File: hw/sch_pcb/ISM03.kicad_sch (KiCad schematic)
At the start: 75 parts, among them J1 JUMP_3X2, J13 HEADER_2x01_PARALLEL, J14 HEADER_2x01_PARALLEL, J15 HEADER_2x01_PARALLEL, J16 HEADER_2x01_PARALLEL, J17 HEADER_2x01_PARALLEL, J19 HEADER_2x01_PARALLEL, J2 MCX, J20 HEADER_2x01_PARALLEL, J21 HEADER_2x01_PARALLEL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

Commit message: Routing WiP.
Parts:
- removed J24, J25: HEADER_1x02, Mlab_Pin_Headers:Straight_1x02, symbol MLAB_HEADER:HEADER_1x02
- removed J26: HEADER_2x01_PARALLEL, Mlab_Pin_Headers:Straight_2x01, symbol MLAB_HEADER:HEADER_2x01_PARALLEL
- removed U1: LM1117-3V3, Mlab_IO:SOT-223, symbol MLAB_U:LM1117
- added J6, J7: HEADER_2x01_PARALLEL, Mlab_Pin_Headers:Straight_2x01, symbol MLAB_HEADER:HEADER_2x01_PARALLEL
- added U1: LM1117MP-3.3, Package_TO_SOT_SMD:SOT-223-3_TabPin2, symbol Regulator_Linear:LM1117MP-3.3
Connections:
- net +3.3V: now also U1.2 (VO)
- net GND: now also U1.1 (GND)
- net VCC: now also U1.3 (VI)
- net at R3.1: now also J7.1, J7.2
- net at R2.1: now also J6.1, J6.2
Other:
- note added: "to GPIO2"
- note added: "to GPIO3"
- moved on the sheet: D2, D3, Q1, Q2, R2, R22, R23, R3

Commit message: Roughtly routet PCB.
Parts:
- removed C10: 8,2pF, Capacitor_SMD:C_0805_2012Metric, symbol Device:C_Small
- removed C8: 15pF, Capacitor_SMD:C_0805_2012Metric, symbol Device:C_Small
- removed L2: 0R, Resistor_SMD:R_0805_2012Metric, symbol Device:L_Small
- removed L4, L6: 18nH, Inductor_SMD:L_0805_2012Metric, symbol Device:L_Small
- C11: value 8,2pF -> 9.1pF
- C12: value 2.7pF -> 2.2pF
- C13: value 5.1pF -> 4.7pF
- C4: value 6.8pf -> 10pF
- C6: value 6.8pf -> 100pF
- C7: value 15pF -> 12pF
- C9: value 8,2pF -> 15pF
- L1: value 0R -> 22nH
- L10: value 56nH -> 62nH
- L3: value 18nH -> 36nH
- L5: value 18nH -> 30nH
- L7: value 39nH -> 33nH; UST_ID 5c70984412875079b91f8809 -> (none)
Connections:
- net GND: no longer C6.2
- net at J3.1: now also C6.2
- net at C6.1: now also C12.2, L9.1
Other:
- note added: "Class-E Match Component Values according to AN648 Split TX/RX Board, 434 MHz."
- note added: "Component values according to AN643 Split TX/RX Board"
- note removed: "Component values are optimised for 433MHz"
- moved on the sheet: C6, J17, R13

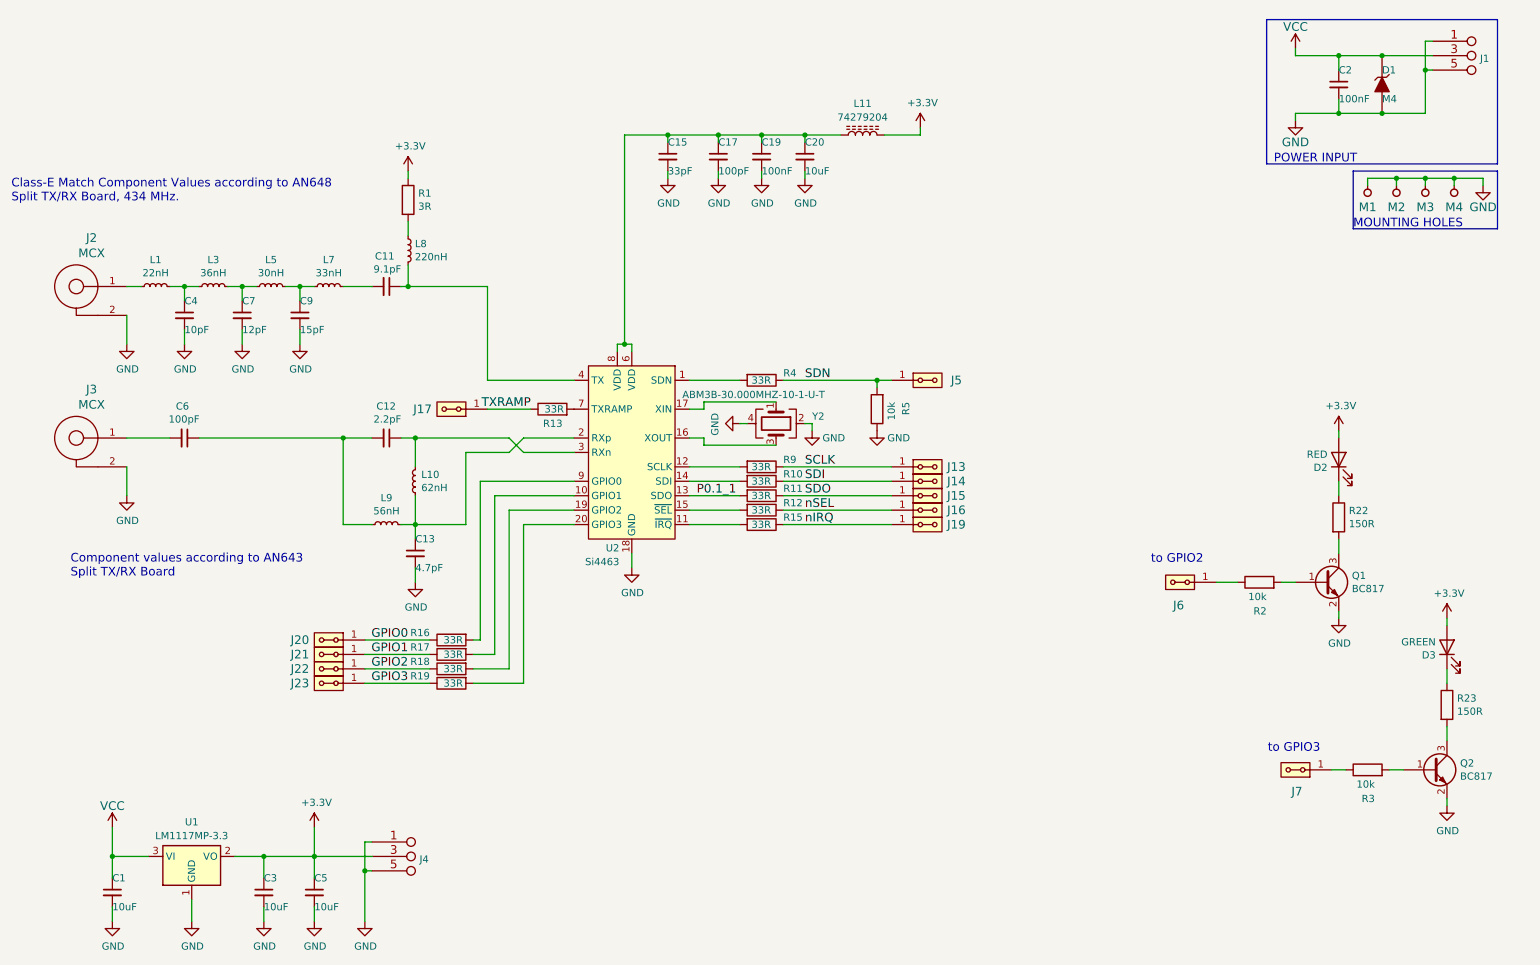
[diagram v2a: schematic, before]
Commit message: Improve Layout, silkscreen Update footprint from libraries.
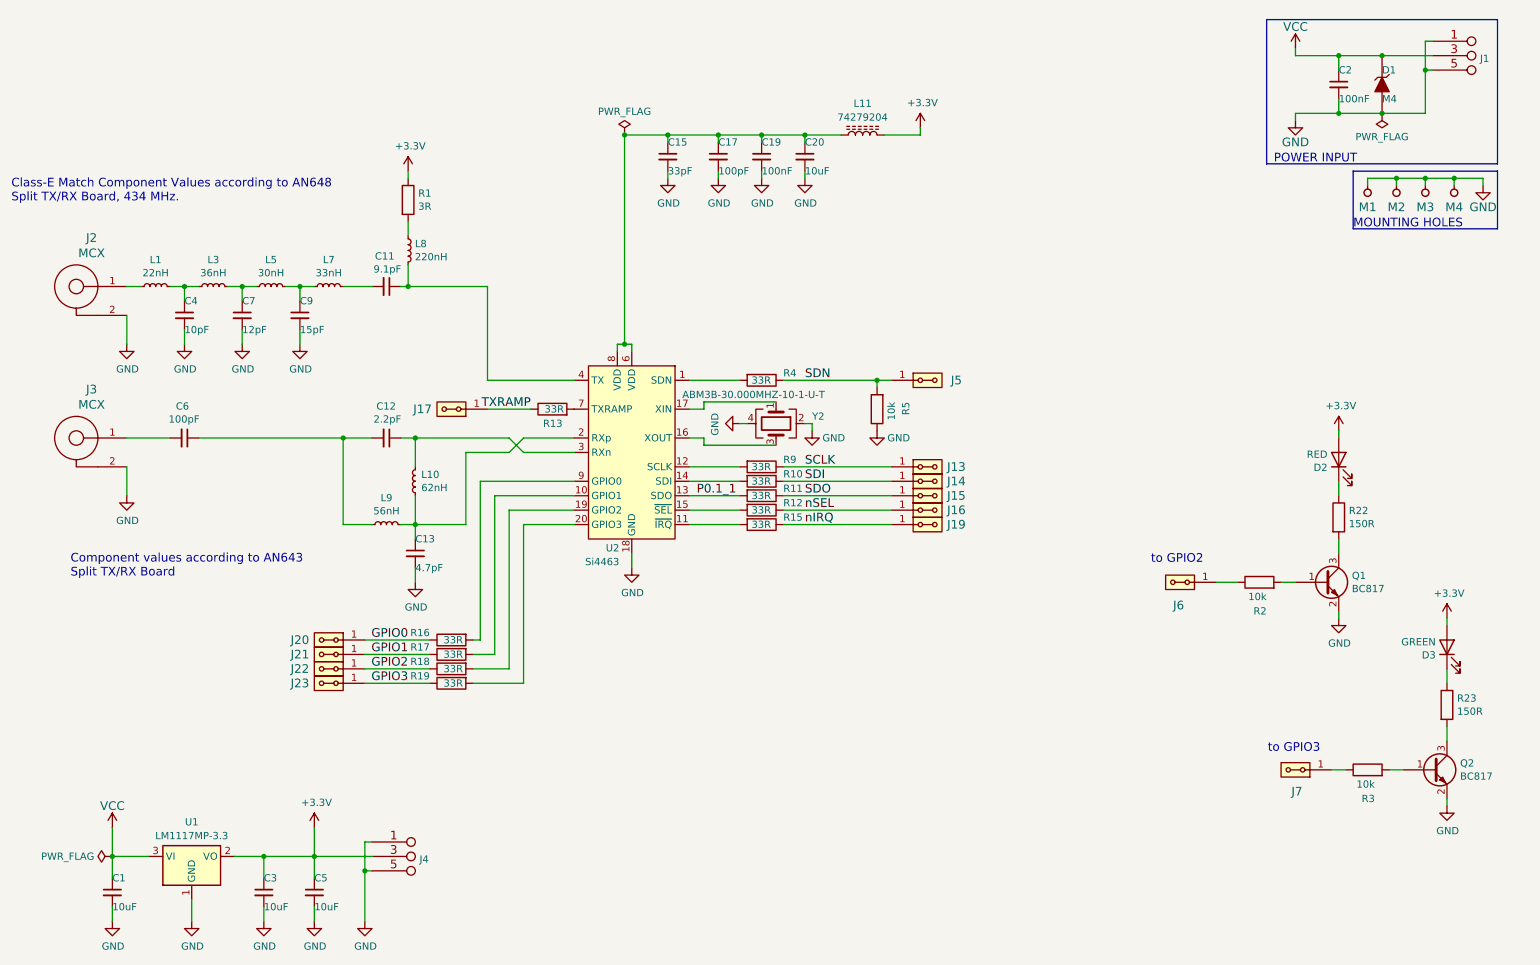
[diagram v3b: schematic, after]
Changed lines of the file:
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@@
 		(rev "ISM01A")
 		(company "Mlab www.mlab.cz")
-		(comment 1 "Sub-GHz ISM radio transceiver")
+		(comment 1 "Sub-GHz ISM radio transceiver\\nwith SPI interface")
 	)
 	(junction
@@
 	)
 	(junction
+		(at 124.46 38.1)
+		(diameter 0)
+		(color 0 0 0 0)
+	)
+	(junction
 		(at 46.99 64.77)
 		(diameter 0)
@@
 	)
 	(symbol
+		(lib_id "power:PWR_FLAG")
+		(at 34.29 165.1 90)
+		(unit 1)
+		(exclude_from_sim no)
+		(in_bom yes)
+		(on_board yes)
+		(dnp no)
+		(fields_autoplaced yes)
+		(property "Reference" "#FLG03"
+			(at 32.385 165.1 0)
+			(effects
+				(font
+					(size 1.27 1.27)
+				)
+				(hide yes)
+			)
+		)
+		(property "Value" "PWR_FLAG"
+			(at 31.1151 165.1 90)
+			(effects
+				(font
+					(size 1.27 1.27)
+				)
+				(justify left)
+			)
+		)
+		(property "Footprint" ""
+			(at 34.29 165.1 0)
+			(effects
+				(font
+					(size 1.27 1.27)
+				)
+				(hide yes)
+			)
+		)
+		(property "Datasheet" "~"
+			(at 34.29 165.1 0)
+			(effects
+				(font
+					(size 1.27 1.27)
+				)
+				(hide yes)
+			)
+		)
+		(property "Description" "Special symbol for telling ERC where power comes from"
+			(at 34.29 165.1 0)
+			(effects
+				(font
+					(size 1.27 1.27)
+				)
+				(hide yes)
+			)
+		)
+		(pin "1"
+		)
+		(instances
+			(project "ISM03"
+				(path "/42713045-fffd-4b2d-ae1e-7232d705fb12"
+					(reference "#FLG03")
+					(unit 1)
+				)
+			)
+		)
+	)
+	(symbol
 		(lib_id "MLAB_HEADER:HEADER_2x01_PARALLEL")
 		(at 222.25 116.84 180)
@@
 	)
 	(symbol
+		(lib_id "power:PWR_FLAG")
+		(at 257.81 34.29 180)
+		(unit 1)
+		(exclude_from_sim no)
+		(in_bom yes)
+		(on_board yes)
+		(dnp no)
+		(fields_autoplaced yes)
+		(property "Reference" "#FLG02"
+			(at 257.81 36.195 0)
+			(effects
+				(font
+					(size 1.27 1.27)
+				)
+				(hide yes)
+			)
+		)
+		(property "Value" "PWR_FLAG"
+			(at 257.81 38.4231 0)
+			(effects
+				(font
+					(size 1.27 1.27)
+				)
+			)
+		)
+		(property "Footprint" ""
+			(at 257.81 34.29 0)
+			(effects
+				(font
+					(size 1.27 1.27)
+				)
+				(hide yes)
+			)
+		)
+		(property "Datasheet" "~"
+			(at 257.81 34.29 0)
+			(effects
+				(font
+					(size 1.27 1.27)
+				)
+				(hide yes)
+			)
+		)
+		(property "Description" "Special symbol for telling ERC where power comes from"
+			(at 257.81 34.29 0)
+			(effects
+				(font
+					(size 1.27 1.27)
+				)
+				(hide yes)
+			)
+		)
+		(pin "1"
+		)
+		(instances
+			(project ""
+				(path "/42713045-fffd-4b2d-ae1e-7232d705fb12"
+					(reference "#FLG02")
+					(unit 1)
+				)
+			)
+		)
+	)
+	(symbol
 		(lib_id "MLAB_HEADER:HEADER_2x01_PARALLEL")
 		(at 177.8 81.28 0)
@@
 					(unit 1)
 				)
+			)
+		)
+	)
+	(symbol
+		(lib_id "power:PWR_FLAG")
+		(at 124.46 38.1 0)
+		(unit 1)
+		(exclude_from_sim no)
+		(in_bom yes)
+		(on_board yes)
+		(dnp no)
+		(fields_autoplaced yes)
+		(property "Reference" "#FLG01"
+			(at 124.46 36.195 0)
+			(effects
+				(font
+					(size 1.27 1.27)
+				)
+				(hide yes)
+			)
+		)
+		(property "Value" "PWR_FLAG"
+			(at 124.46 33.9669 0)
+			(effects
+				(font
+					(size 1.27 1.27)
+				)
+			)
+		)
+		(property "Footprint" ""
+			(at 124.46 38.1 0)
+			(effects
+				(font
+					(size 1.27 1.27)
+				)
+				(hide yes)
+			)
+		)
+		(property "Datasheet" "~"
+			(at 124.46 38.1 0)
+			(effects
+				(font
+					(size 1.27 1.27)
+				)
+				(hide yes)
+			)
+		)
+		(property "Description" "Special symbol for telling ERC where power comes from"
+			(at 124.46 38.1 0)
+			(effects
+				(font
+					(size 1.27 1.27)
+				)
+				(hide yes)
+			)
+		)
+		(pin "1"
+		)
+		(instances
+			(project ""
+				(path "/42713045-fffd-4b2d-ae1e-7232d705fb12"
+					(reference "#FLG01")
+					(unit 1)
+				)

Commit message: Update components identification.
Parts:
- C11: UST_ID 5c70984712875079b91f8b2f -> 611b60e71287500165a9732d
- C12: UST_ID 5c70984712875079b91f8b28 -> 5c70984712875079b91f8b27
- C13: UST_ID 5c70984812875079b91f8ba2 -> 5c70984712875079b91f8b2c
- C4: UST_ID 5c70984712875079b91f8b2e -> 5c70984712875079b91f8b30
- C6: UST_ID 5c70984712875079b91f8b2e -> 5c70984712875079b91f8b3b
- C7: UST_ID 5c70984712875079b91f8b32 -> 5c70984712875079b91f8b31
- C9: UST_ID 5c70984712875079b91f8b2f -> 5c70984712875079b91f8b32
- L1: UST_ID 5c70984512875079b91f896b -> 60be80ed1287500165e6c3bb
- L10: UST_ID 5c70984812875079b91f8ba4 -> 64c92bf976c82a1d3b57944c
- L3: UST_ID 5c70984412875079b91f8806 -> 66a10bc36fdfe6f54e2ebbf8
- L5: UST_ID 5c70984412875079b91f8806 -> 611b69d31287500165a9742b
- L7: UST_ID (none) -> 5c70984412875079b91f8808
- R2, R3, R5: UST_ID 5c70984512875079b91f897a -> 5c70984612875079b91f899f
- U2: UST_ID (none) -> 5c70984612875079b91f8a0a
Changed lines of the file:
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@@
 			)
 		)
-		(property "UST_ID" "5c70984512875079b91f896b"
+		(property "UST_ID" "60be80ed1287500165e6c3bb"
 			(at 41.91 64.77 0)
 			(effects
@@
 			)
 		)
-		(property "UST_ID" "5c70984412875079b91f8806"
+		(property "UST_ID" "66a10bc36fdfe6f54e2ebbf8"
 			(at 52.07 64.77 0)
 			(effects
@@
 			)
 		)
-		(property "UST_ID" "5c70984412875079b91f8806"
+		(property "UST_ID" "611b69d31287500165a9742b"
 			(at 62.23 64.77 0)
 			(effects
@@
 			)
 		)
-		(property "UST_ID" ""
+		(property "UST_ID" "5c70984412875079b91f8808"
 			(at 72.39 64.77 0)
 			(effects
@@
 			)
 		)
-		(property "UST_ID" "5c70984712875079b91f8b2f"
+		(property "UST_ID" "611b60e71287500165a9732d"
 			(at 82.55 64.77 0)
 			(effects
@@
 			)
 		)
-		(property "UST_ID" "5c70984712875079b91f8b2e"
+		(property "UST_ID" "5c70984712875079b91f8b30"
 			(at 46.99 69.85 0)
 			(effects
@@
 			)
 		)
-		(property "UST_ID" "5c70984712875079b91f8b32"
+		(property "UST_ID" "5c70984712875079b91f8b31"
 			(at 57.15 69.85 0)
 			(effects
@@
 			)
 		)
-		(property "UST_ID" "5c70984712875079b91f8b2f"
+		(property "UST_ID" "5c70984712875079b91f8b32"
 			(at 67.31 69.85 0)
 			(effects
@@
 			)
 		)
-		(property "UST_ID" "5c70984712875079b91f8b2e"
+		(property "UST_ID" "5c70984712875079b91f8b3b"
 			(at 46.99 91.44 0)
 			(effects
@@
 			)
 		)
-		(property "UST_ID" "5c70984812875079b91f8ba4"
+		(property "UST_ID" "64c92bf976c82a1d3b57944c"
 			(at 87.63 99.06 0)
 			(effects
@@
 			)
 		)
-		(property "UST_ID" "5c70984812875079b91f8ba2"
+		(property "UST_ID" "5c70984712875079b91f8b2c"
 			(at 87.63 111.76 0)
 			(effects
@@
 			)
 		)
-		(property "UST_ID" "5c70984712875079b91f8b28"
+		(property "UST_ID" "5c70984712875079b91f8b27"
 			(at 82.55 91.44 0)
 			(effects
@@
 			)
 		)
-		(property "UST_ID" "5c70984512875079b91f897a"
+		(property "UST_ID" "5c70984612875079b91f899f"
 			(at 168.91 86.36 0)
 			(effects
@@
 			)
 		)
+		(property "UST_ID" "5c70984612875079b91f8a0a"
+			(at 125.73 93.98 0)
+			(effects
+				(font
+					(size 1.27 1.27)
+				)
+				(hide yes)
+			)
+		)
 		(pin "2"
 		)
@@
 			)
 		)
-		(property "UST_ID" "5c70984512875079b91f897a"
+		(property "UST_ID" "5c70984612875079b91f899f"
 			(at 255.27 149.86 0)
 			(effects
@@
 			)
 		)
-		(property "UST_ID" "5c70984512875079b91f897a"
+		(property "UST_ID" "5c70984612875079b91f899f"
 			(at 236.22 116.84 0)
 			(effects

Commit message: Fix inductor type.
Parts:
- L10: UST_ID 64c92bf976c82a1d3b57944c -> 66a127196fdfe6f54e2ebd35
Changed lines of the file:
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@@
 			)
 		)
-		(property "UST_ID" "64c92bf976c82a1d3b57944c"
+		(property "UST_ID" "66a127196fdfe6f54e2ebd35"
 			(at 87.63 99.06 0)
 			(effects
